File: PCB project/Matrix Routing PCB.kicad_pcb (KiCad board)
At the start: 2 copper layers, 80 x 50.6 mm, 4 parts, among them J1 Connector 1x6, J2 JST_PH_S4B-PH-SM4-TB_1x04-1MP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, J3 ESQ-105-23-T-D, U1 FT232RL

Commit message: Schematic finish
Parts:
- added J4: TSM-102-01-L-DH-A, Matrix Routing PCB:SAMTEC_TSM-102-01-L-DH-A, F.Cu at (134.0, 49.0)
- added J5: USB-A-S-X-X-SM2-R, Matrix Routing PCB:SAMTEC_USB-A-S-X-X-SM2-R, F.Cu at (84.0, 59.9)
- J1: value Connector 1x6 -> 53261-0471; moved to F.Cu
- J2: value JST_PH_S4B-PH-SM4-TB_1x04-1MP_P2.00mm_Horizontal -> JST_PH_S4B-PH-SM4-TB; moved to F.Cu
- moved J1 48.6 mm to (101.9, 97.0)
- moved U1 18.0 mm to (83.7, 82.4)
- moved J3 8.71 mm to (127.1, 67.9)
- moved J2 1.31 mm to (66.9, 75.5), turned to -90 degrees
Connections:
- J1 pad 1: unconnected-(J1-Pin_1-Pad1) -> +5V
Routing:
- net GND: track 0.00 -> 0.85 mm

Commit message: House keeping changes
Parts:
- added C1: 100nF, Capacitor_SMD:C_0603_1608Metric, F.Cu at (90.6, 83.9)
- added C2: 10nF, Capacitor_SMD:C_0603_1608Metric, F.Cu at (76.8, 81.2)
- added C3: 100nF, Capacitor_SMD:C_0603_1608Metric, F.Cu at (90.6, 80.9)
- added C4: 4.7uF, Capacitor_SMD:C_0603_1608Metric, F.Cu at (92.1, 80.9)
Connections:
- J2 pad 2: unconnected-(J2-Pin_2-Pad2) -> /RX_FTDI_TX_BOARD
- J2 pad 3: unconnected-(J2-Pin_3-Pad3) -> /TX_FTDI_RX_BOARD
- J2 pad 4: unconnected-(J2-Pin_4-Pad4) -> GND
- U1 pad 1: unconnected-(U1-TXD-Pad1) -> /TX_FTDI_RX_BOARD
- U1 pad 17: unconnected-(U1-3V3OUT-Pad17) -> Net-(U1-3V3OUT)
- U1 pad 18: unconnected-(U1-GND-Pad18) -> GND
- U1 pad 20: unconnected-(U1-VCC-Pad20) -> +5V
- U1 pad 21: unconnected-(U1-GND-Pad21) -> GND
- U1 pad 25: unconnected-(U1-AGND-Pad25) -> GND
- U1 pad 4: unconnected-(U1-VCCIO-Pad4) -> +5V
- U1 pad 5: unconnected-(U1-RXD-Pad5) -> /RX_FTDI_TX_BOARD
- U1 pad 7: unconnected-(U1-GND-Pad7) -> GND

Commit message: Placement to review
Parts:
- J2: footprint Matrix Routing PCB:JST_PH_S4B-PH-SM4-TB_1x04-1MP_P2.00mm_Horizontal -> Matrix Routing PCB:S4BXHSM4TBLFSN
- J3: moved to F.Cu
- moved C1 88.1 mm to (172.4, 116.6)
- moved C3 88.1 mm to (172.4, 113.6)
- moved C4 88.1 mm to (173.9, 113.6)
- moved C2 88.1 mm to (158.6, 113.9)
- moved U1 88.1 mm to (165.5, 115.1)
- moved J4 81.8 mm to (191.1, 107.6)
- moved J3 71.1 mm to (184.2, 110.3)
- moved J2 66.4 mm to (114.1, 122.2)
- moved J5 63.2 mm to (126.3, 106.9)
- moved J1 58.3 mm to (150.5, 129.2)
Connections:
- J1 pad 2: /USB2_DN -> /USB1_DN
- J1 pad 3: /USB2_DP -> /USB1_DP
- U1 pad 15: /USB1_DP -> /USB2_DP
- U1 pad 16: /USB1_DN -> /USB2_DN
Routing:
- net /USB1_DP: track 0.00 -> 8.04 mm
- net /USB1_DN: track 0.00 -> 7.30 mm
- net GND: track 0.85 -> 0.00 mm
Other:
- board size 80 x 50.6 mm -> 87 x 35 mm
- board text added: "What is the part number of the device used in the moc pcb"

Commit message: Placement is done and 3D generated
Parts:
- added FID1: Fiducial, Fiducial:Fiducial_0.5mm_Mask1.5mm, F.Cu at (112.3, 102.0)
- added FID2: Fiducial, Fiducial:Fiducial_0.5mm_Mask1.5mm, F.Cu at (112.4, 128.1)
- added FID3: Fiducial, Fiducial:Fiducial_0.5mm_Mask1.5mm, F.Cu at (184.8, 127.6)
- added H1: MountingHole, MountingHole:MountingHole_3.2mm_M3, F.Cu at (137.6, 102.0)
- J2: footprint Matrix Routing PCB:S4BXHSM4TBLFSN -> Matrix Routing PCB:JST_PH_S4B-PH-SM4-TB_1x04-1MP_P2.00mm_Horizontal
- moved J2 4.31 mm to (113.2, 118.0)
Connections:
- J2 pad MP1: unconnected-(J2-PadMP1) -> (no net)
- J2 pad MP2: unconnected-(J2-PadMP2) -> (no net)
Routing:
- net /USB1_DP: track 8.04 -> 0.00 mm
- net /USB1_DN: track 7.30 -> 0.00 mm
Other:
- outline, holes or cut-outs redrawn
- board text removed: "What is the part number of the device used in the moc pcb"

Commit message: Clear J5 second hole
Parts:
- C1, C3: value 100nF -> C
- C2: value 10nF -> C
- C4: value 4.7uF -> C
- J1: value 53261-0471 -> Connector 1x6
- J2: value JST_PH_S4B-PH-SM4-TB -> JST_PH_S4B-PH-SM4-TB_1x04-1MP_P2.00mm_Horizontal
- J3: value ESQ-105-23-T-D -> ESQ-105-11-T-D
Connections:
- J2 pad MP1: (no net) -> unconnected-(J2-PadMP1)
- J2 pad MP2: (no net) -> unconnected-(J2-PadMP2)
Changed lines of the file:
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@@
 			)
 		)
-		(property "Value" "JST_PH_S4B-PH-SM4-TB"
+		(property "Value" "JST_PH_S4B-PH-SM4-TB_1x04-1MP_P2.00mm_Horizontal"
 			(at 0 5.8 90)
 			(layer "F.Fab")
@@
 		(sheetname "/")
 		(sheetfile "Matrix Routing PCB.kicad_sch")
-		(attr smd)
+		(units
+			(unit
+				(name "A")
+				(pins "1" "2" "3" "4" "MP1" "MP2")
+			)
+		)
+		(attr smd dnp)
 		(duplicate_pad_numbers_are_jumpers no)
 		(fp_line
@@
 			(layers "F.Cu" "F.Mask" "F.Paste")
 			(roundrect_rratio 0.166667)
+			(net "unconnected-(J2-PadMP1)")
+			(pinfunction "MP1_MP1")
+			(pintype "passive+no_connect")
 		)
 		(pad "MP2" smd roundrect
@@
 			(layers "F.Cu" "F.Mask" "F.Paste")
 			(roundrect_rratio 0.166667)
+			(net "unconnected-(J2-PadMP2)")
+			(pinfunction "MP2_MP2")
+			(pintype "passive+no_connect")
 		)
 		(embedded_fonts no)
@@
 			)
 		)
-		(property "Value" "100nF"
+		(property "Value" "C"
 			(at 0 1.43 90)
 			(layer "F.Fab")
@@
 			)
 		)
-		(property "Value" "4.7uF"
+		(property "Value" "C"
 			(at 0 1.43 90)
 			(layer "F.Fab")
@@
 			)
 		)
-		(property "Value" "ESQ-105-23-T-D"
+		(property "Value" "ESQ-105-11-T-D"
 			(at -0.314556 4.446355 90)
 			(layer "F.Fab")
@@
 			)
 		)
-		(property "Value" "10nF"
+		(property "Value" "C"
 			(at 0 1.43 90)
 			(layer "F.Fab")
@@
 		)
 		(property "Value" "TSM-102-01-L-DH-A"
-			(at 11.7 11.95 0)
+			(at 3.7 6.4 90)
 			(layer "F.Fab")
 			(effects
@@
 		(sheetname "/")
 		(sheetfile "Matrix Routing PCB.kicad_sch")
-		(units
-			(unit
-				(name "A")
-				(pins "01" "03" "02" "04")
-			)
-		)
-		(attr smd)
+		(attr smd dnp)
 		(duplicate_pad_numbers_are_jumpers no)
 		(fp_line
@@
 			(layers "*.Cu" "*.Mask")
 		)
-		(pad "" np_thru_hole circle
-			(at 0 0)
-			(size 1.78 1.78)
-			(drill 1.78)
-			(layers "*.Cu" "*.Mask")
-		)
 		(pad "01" smd rect
 			(at 1.27 4.305)
@@
 		)
 		(embedded_fonts no)
-		(embedded_files
-			(file
-				(name "TSM-102-01-L-DH-A.stp")
-				(type model)
-				(checksum "0429DFA1EE017D3F440888B53996B3A1")
-			)
-		)
-		(model "kicad-embed://TSM-102-01-L-DH-A.stp"
-			(offset
-				(xyz 0 0 1.5)
-			)
-			(scale
-				(xyz 1 1 1)
-			)
-			(rotate
-				(xyz -90 -0 -180)
-			)
-		)
 	)
 	(footprint "Matrix Routing PCB:SAMTEC_USB-A-S-X-X-SM2-R"
@@
 			)
 		)
-		(attr smd)
+		(attr smd dnp)
 		(duplicate_pad_numbers_are_jumpers no)
 		(fp_line
@@
 			)
 		)
-		(property "Value" "100nF"
+		(property "Value" "C"
 			(at 0 1.43 90)
 			(layer "F.Fab")
@@
 			)
 		)
-		(property "Value" "53261-0471"
+		(property "Value" "Connector 1x6"
 			(at 0.3 -4.9 0)
 			(layer "F.Fab")

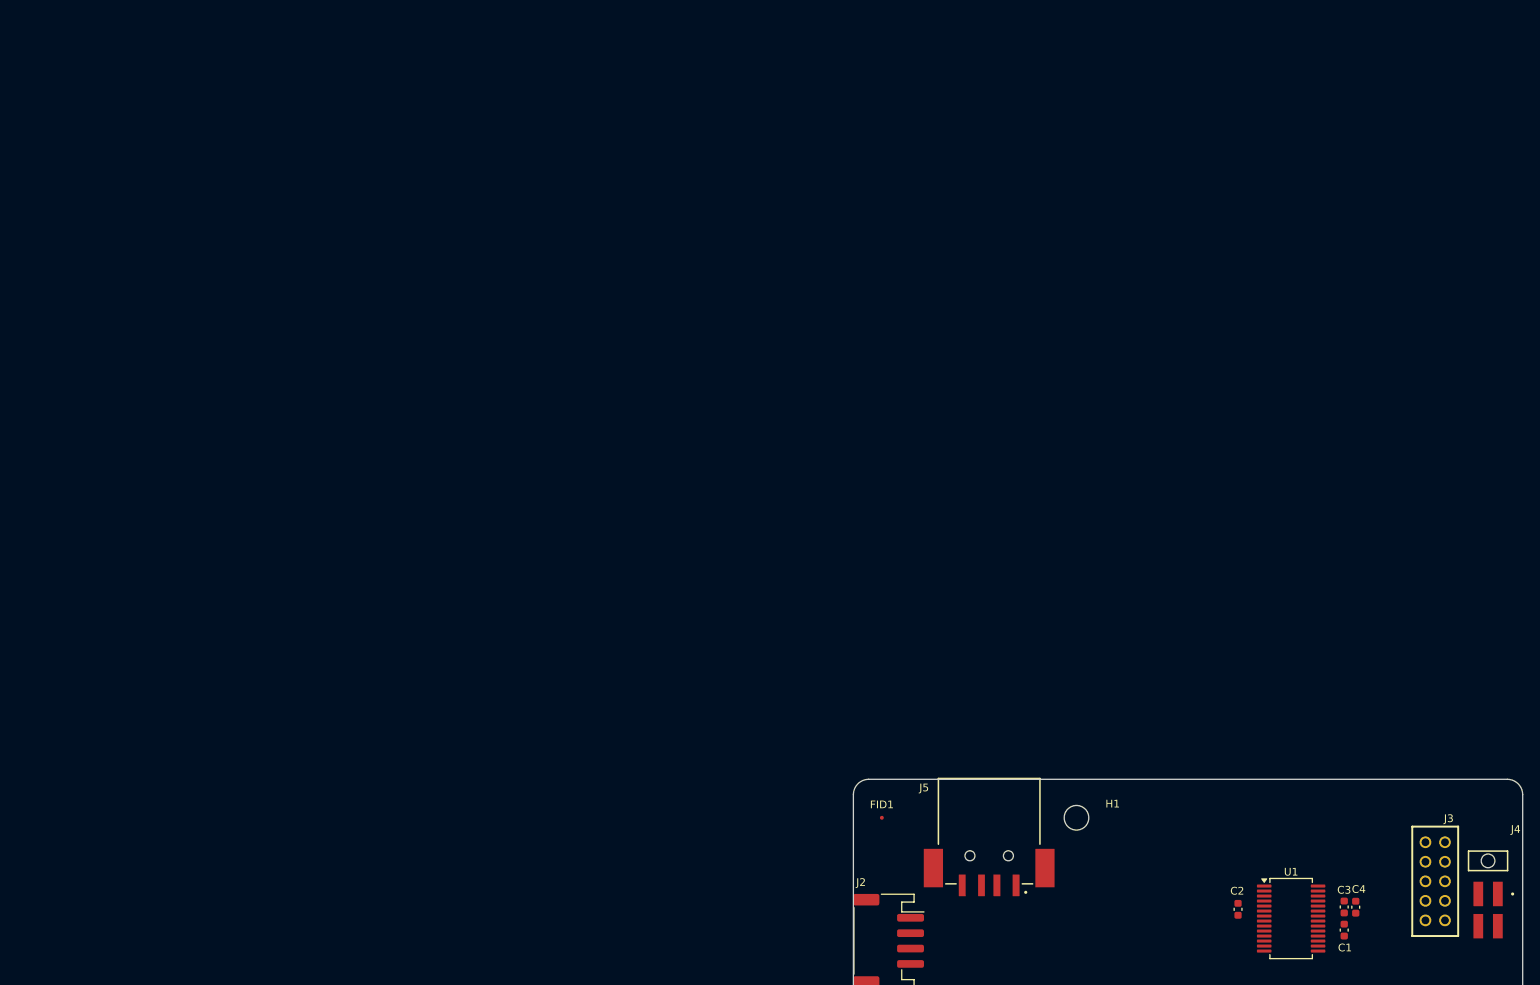
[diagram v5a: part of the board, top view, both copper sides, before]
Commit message: Make J2 and J5 part of the project library
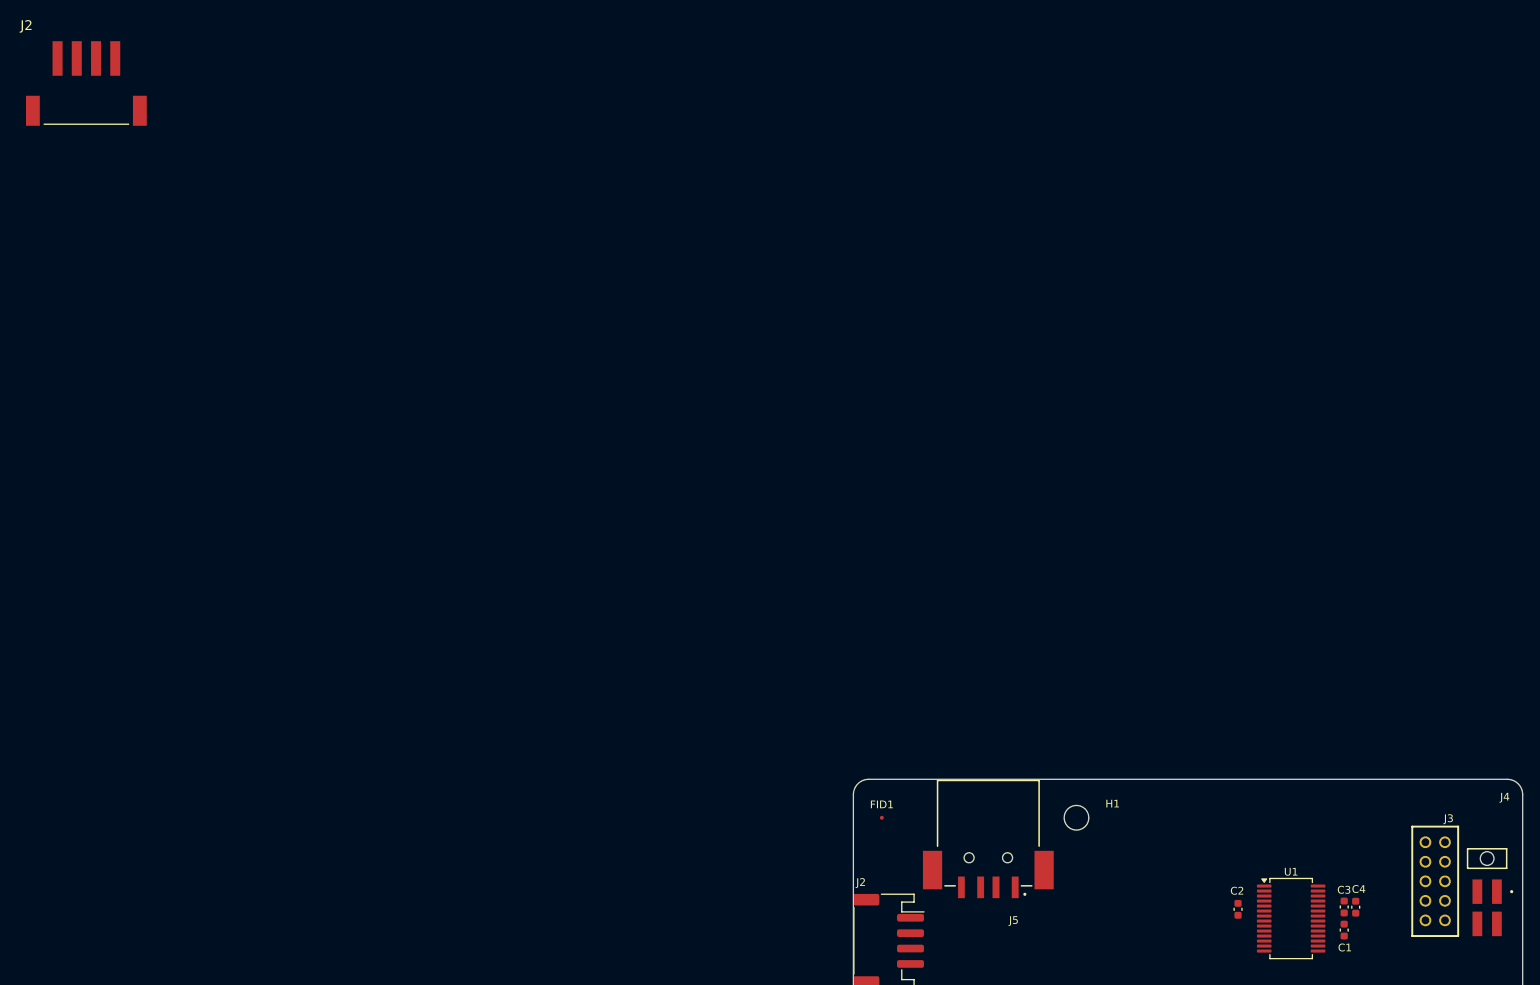
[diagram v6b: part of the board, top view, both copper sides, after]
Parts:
- added J2: JST_PH_S4B-PH-SM4-TB_1x04-1MP_P2.00mm_Horizontal, Matrix Routing PCB:S4BXHSM4TBLFSN, F.Cu at (8.90, 7.58)
- moved J4 0.32 mm to (191.0, 107.3)
- moved J5 0.28 mm to (126.1, 107.2)

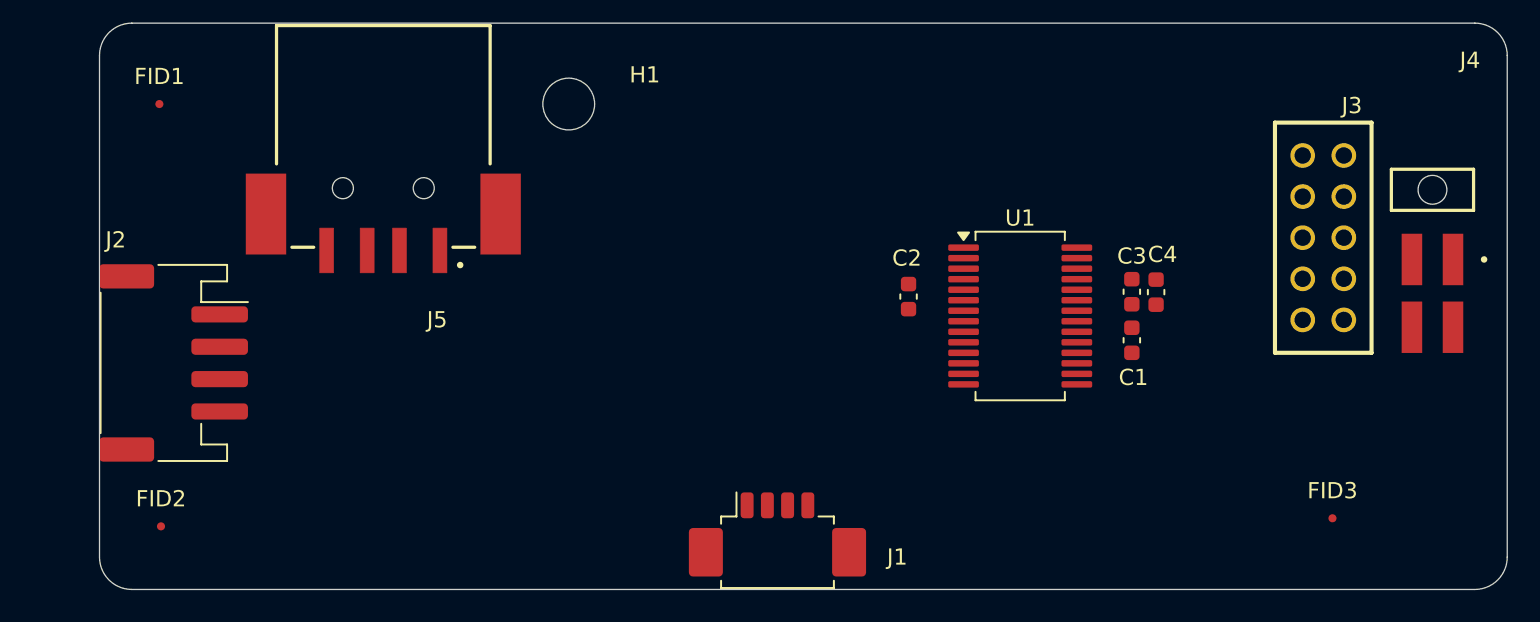
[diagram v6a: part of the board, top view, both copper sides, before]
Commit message: Adding the netclasses, and physical board and track and gap
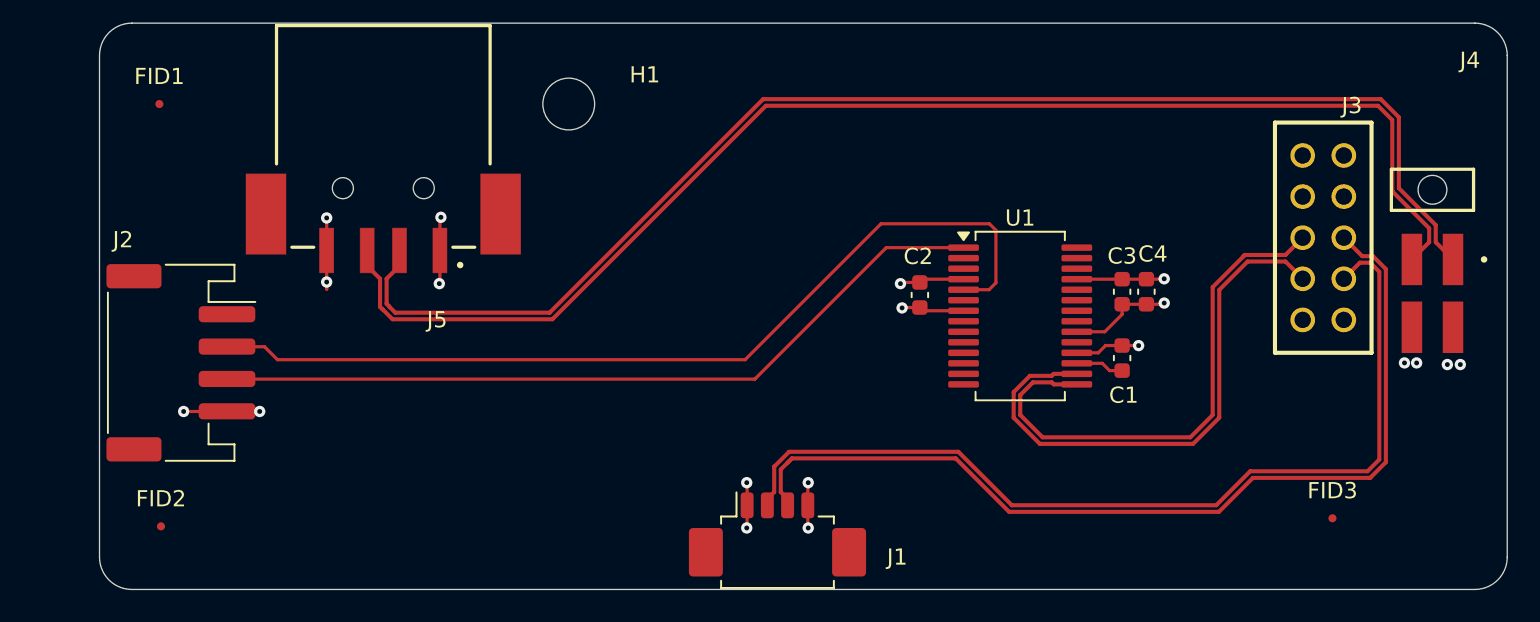
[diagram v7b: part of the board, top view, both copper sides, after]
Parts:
- moved C1 1.25 mm to (171.8, 117.7)
- moved C2 0.71 mm to (159.3, 113.8)
- moved C4 0.60 mm to (173.3, 113.6)
- moved C3 0.60 mm to (171.8, 113.6)
- moved J2 0.46 mm to (113.6, 118.0)
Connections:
- J4 pad 01: VBUS -> /USB_OTG_DN
- J4 pad 02: /USB_OTG_DP -> VBUS
- J4 pad 03: GND -> /USB_OTG_DP
- J4 pad 04: /USB_OTG_DN -> GND
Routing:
- net /USB_OTG_DP: track 0.00 -> 82.5 mm
- net /USB_OTG_DN: track 0.00 -> 82.5 mm
- net /USB1_DP: track 0.00 -> 58.2 mm
- net /USB1_DN: track 0.00 -> 57.3 mm
- net /RX_FTDI_TX_BOARD: track 0.00 -> 56.9 mm
- net /TX_FTDI_RX_BOARD: track 0.00 -> 48.9 mm
- net /USB2_DN: track 0.00 -> 34.2 mm
- net /USB2_DP: track 0.00 -> 32.9 mm
- net GND: track 0.00 -> 26.9 mm, vias 0 -> 11
- net +5V: track 0.00 -> 13.3 mm, vias 0 -> 4
- net VBUS: track 0.00 -> 4.14 mm, vias 0 -> 2
- net Net-(U1-3V3OUT): track 0.00 -> 2.99 mm
- net (no net): vias 0 -> 2
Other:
- copper layers 2 -> 4

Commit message: Routing, no DRC errors just warnings
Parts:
- removed the J2 at (8.90, 7.58)
- moved H1 71.0 mm to (203.9, 76.6)
- moved J2 71.0 mm to (179.9, 92.6)
- moved J3 71.0 mm to (250.5, 84.8)
- moved J4 71.0 mm to (257.3, 81.9)
- moved U1 71.0 mm to (231.8, 89.7)
- moved FID1 71.0 mm to (178.6, 76.6)
- moved J1 71.0 mm to (216.8, 103.8)
- moved J5 71.0 mm to (192.4, 81.8)
- moved C1 71.0 mm to (238.1, 92.3)
- moved C2 71.0 mm to (225.6, 88.4)
- moved C3 71.0 mm to (238.1, 88.2)
- moved C4 71.0 mm to (239.6, 88.2)
- moved FID2 71.0 mm to (178.7, 102.7)
- moved FID3 71.0 mm to (251.1, 102.2)
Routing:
- net GND: track 26.9 -> 42.4 mm, vias 11 -> 16
- net VBUS: track 4.14 -> 8.86 mm, vias 2 -> 4
- net (no net): vias 2 -> 0
- added copper zone on B.Cu, net +5V
- added copper zone on In1.Cu, net GND
- added copper zone on B.Cu, net VBUS
